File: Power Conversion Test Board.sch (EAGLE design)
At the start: 44 parts, among them U1 LM2678, U2 LM2678

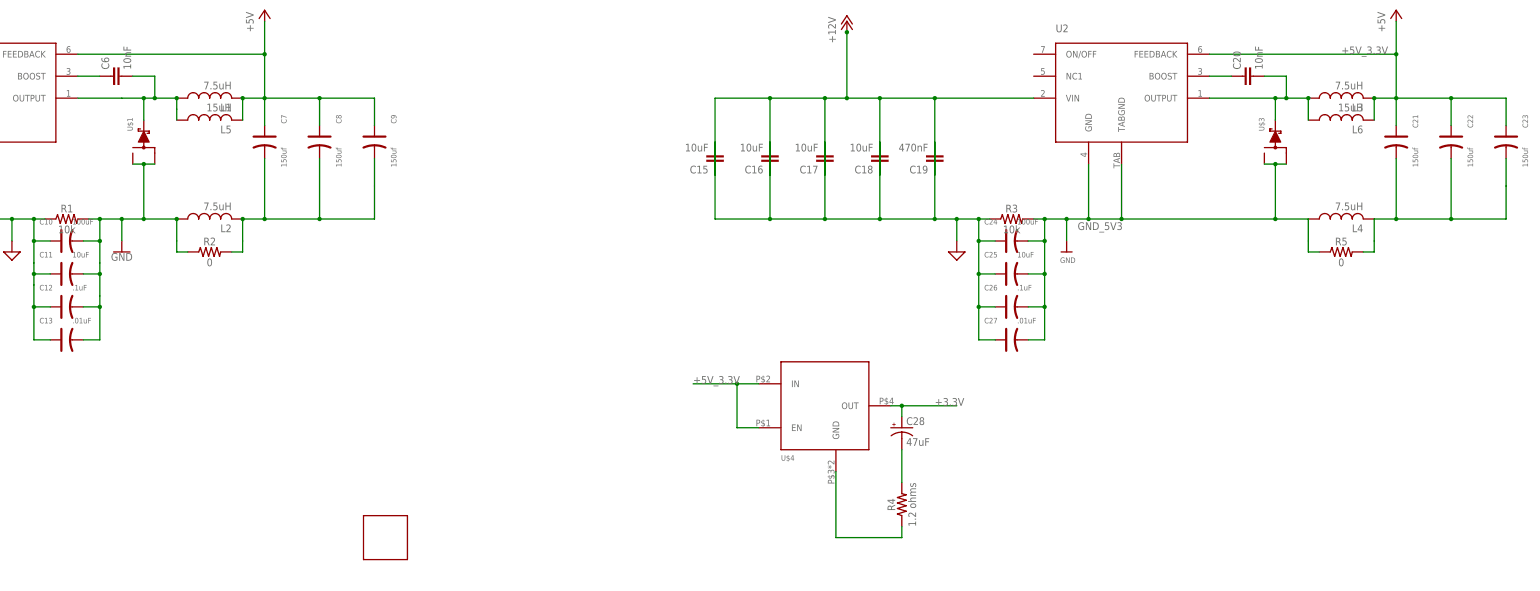
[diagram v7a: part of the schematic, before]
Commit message: lots of things
put in board outline, also fixed the inductors because they were the wrong ones
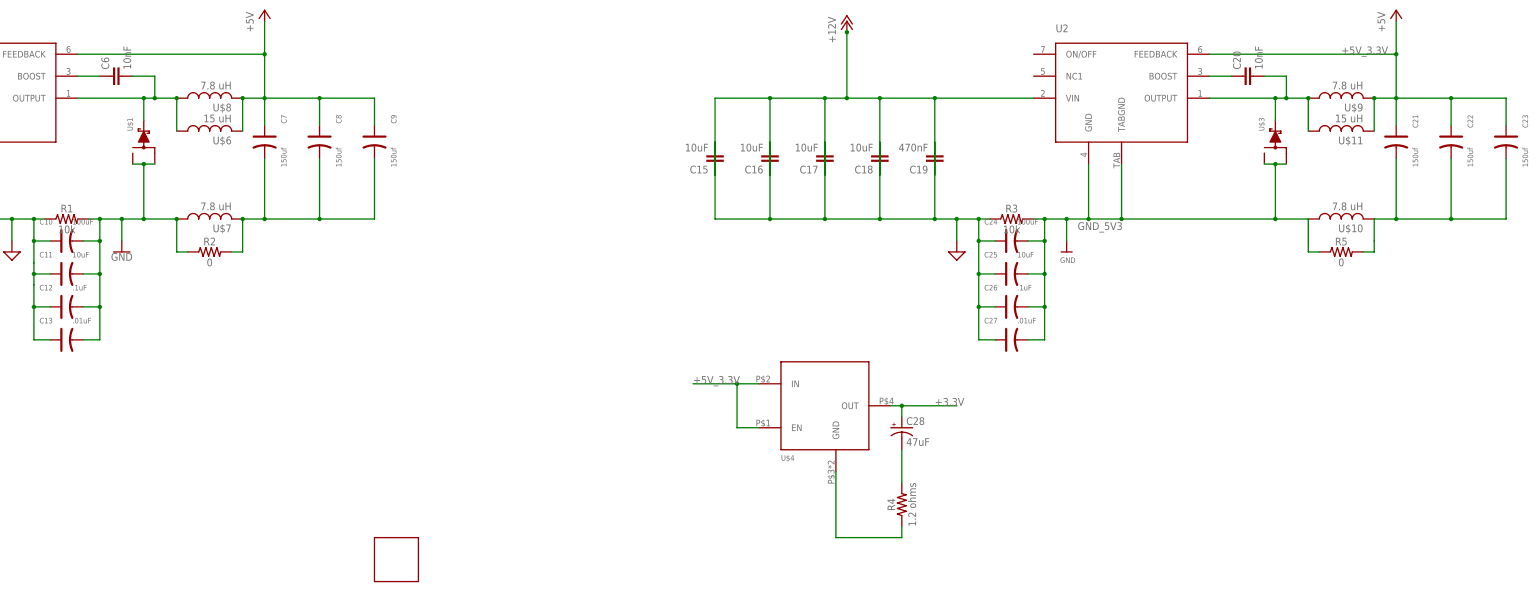
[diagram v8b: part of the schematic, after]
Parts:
- removed L1, L2, L3, L4: 7.5uH, rcl:L-USL2012C
- removed L5, L6: 15uH, rcl:L-USL2012C
- added U$10, U$7, U$8, U$9: 7.8 uH, DiscreteComponents:HCMA1305
- added U$11, U$6: 15 uH, DiscreteComponents:HCMA1305
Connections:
- net +5V: now also U$6.2, U$8.2; no longer L1.2, L5.2
- net +5V_3.3V: now also U$11.2, U$9.2; no longer L3.2, L6.2
- net GND_5V: now also U$7.1; no longer L2.1
- net GND_5V3: now also U$10.1; no longer L4.1
- net N$1: now also U$6.1, U$8.1; no longer L1.1, L5.1
- net N$6: now also U$10.2; no longer L4.2
- net N$7: now also U$11.1, U$9.1; no longer L3.1, L6.1
- net N$8: now also U$7.2; no longer L2.2
